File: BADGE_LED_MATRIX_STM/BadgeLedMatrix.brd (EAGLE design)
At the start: 100 x 50 mm, 111 parts, among them CN2 MICRO-USB-5P-340015001, IC1 STM32F0P, IC2 REG1117, Q1 12MHz, Q2 8MHz, U1 USBLC6SOT-23

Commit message: Fix for connection of VCC from shift registers
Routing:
- net BTN3: track 23.1 -> 28.7 mm
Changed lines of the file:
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@@
 <via x="36.83" y="42.545" extent="1-16" drill="0.8" diameter="0.6096"/>
 <wire x1="34.29" y1="16.51" x2="40.005" y2="19.05" width="0.8128" layer="1"/>
-<contactref element="ROWS" pad="16"/>
 <contactref element="ROWS" pad="10"/>
 <wire x1="47.625" y1="15.5" x2="47.625" y2="13.335" width="0.4064" layer="1"/>
-<wire x1="40.005" y1="15.5" x2="40.005" y2="19.05" width="0.4064" layer="1"/>
-<contactref element="COLUMNS" pad="16"/>
 <contactref element="COLUMNS" pad="10"/>
 <wire x1="45.085" y1="42.545" x2="46.99" y2="42.545" width="0.4064" layer="1"/>
@@
 <wire x1="34.29" y1="16.51" x2="34.29" y2="8.89" width="0.8128" layer="1"/>
 <wire x1="32.385" y1="6.985" x2="19.685" y2="6.985" width="0.8128" layer="1"/>
-<wire x1="36.83" y1="42.545" x2="36.83" y2="43.815" width="0.6096" layer="1"/>
-<wire x1="36.83" y1="43.815" x2="38.1" y2="45.085" width="0.6096" layer="1"/>
-<wire x1="38.1" y1="45.085" x2="39.63" y2="45.085" width="0.6096" layer="1"/>
-<wire x1="39.63" y1="45.085" x2="40.005" y2="44.71" width="0.6096" layer="1"/>
+<wire x1="36.83" y1="42.545" x2="36.83" y2="44.03" width="0.6096" layer="1"/>
 <contactref element="PRG" pad="1"/>
 <contactref element="PRG" pad="2"/>
@@
 <wire x1="10.2" y1="22.2" x2="11.595" y2="22.2" width="0.4064" layer="1"/>
 <wire x1="11.595" y1="22.2" x2="16.185" y2="17.61" width="0.4064" layer="1"/>
+<contactref element="COLUMNS" pad="16"/>
+<contactref element="ROWS" pad="16"/>
+<wire x1="36.83" y1="44.03" x2="37.8" y2="45" width="0.6096" layer="1"/>
+<wire x1="37.8" y1="45" x2="39.715" y2="45" width="0.6096" layer="1"/>
+<wire x1="39.715" y1="45" x2="40.005" y2="44.71" width="0.6096" layer="1"/>
+<wire x1="40.005" y1="15.5" x2="40.005" y2="19.05" width="0.6096" layer="1"/>
 </signal>
 <signal name="C0">
@@
 <wire x1="32.385" y1="31.115" x2="31.75" y2="31.75" width="0.3048" layer="1"/>
 <wire x1="31.75" y1="31.75" x2="31.75" y2="41.91" width="0.3048" layer="1"/>
-<wire x1="32.345" y1="14.351" x2="32.345" y2="19.939" width="0" layer="19" extent="1-1"/>
+<wire x1="32.345" y1="19.939" x2="32.345" y2="14.351" width="0.3048" layer="1"/>
 </signal>
 <signal name="BTN4">

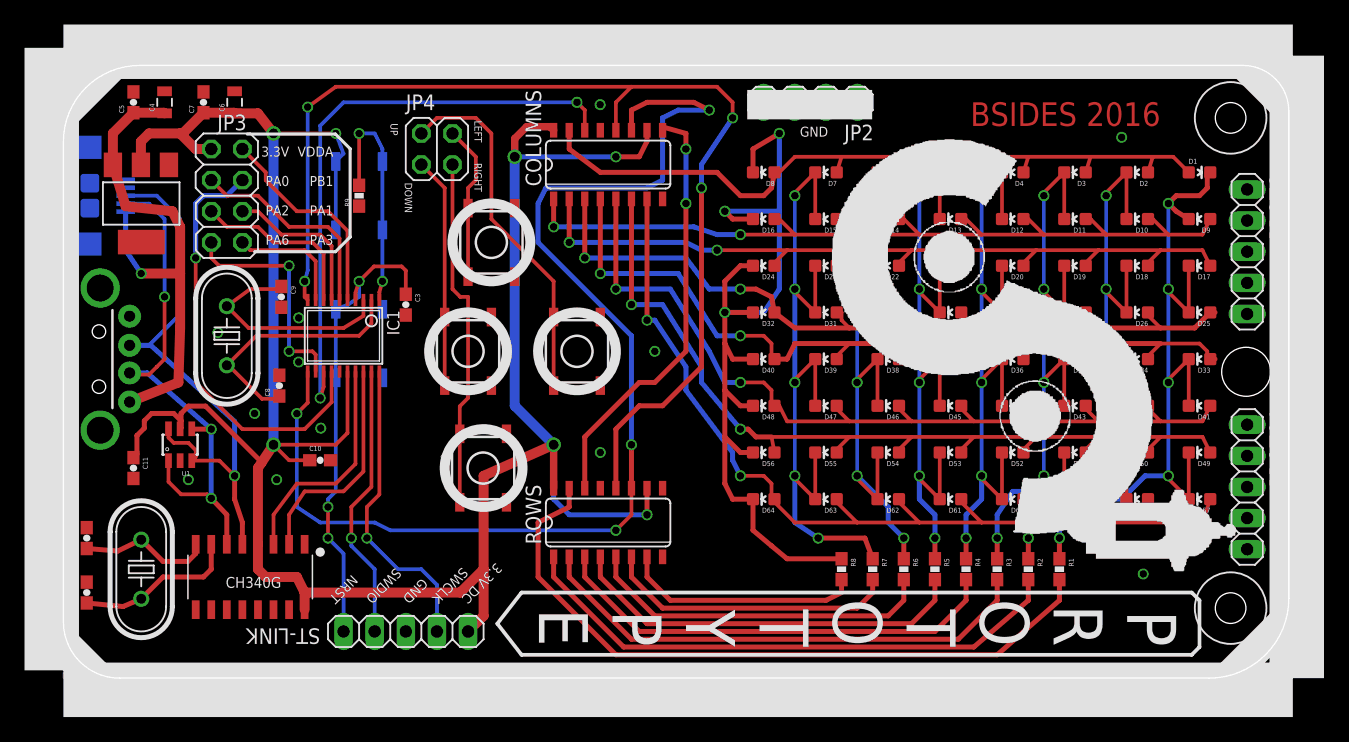
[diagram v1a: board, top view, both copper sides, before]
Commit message: Board diode orientation fix, board corners, allignment of top corner holes
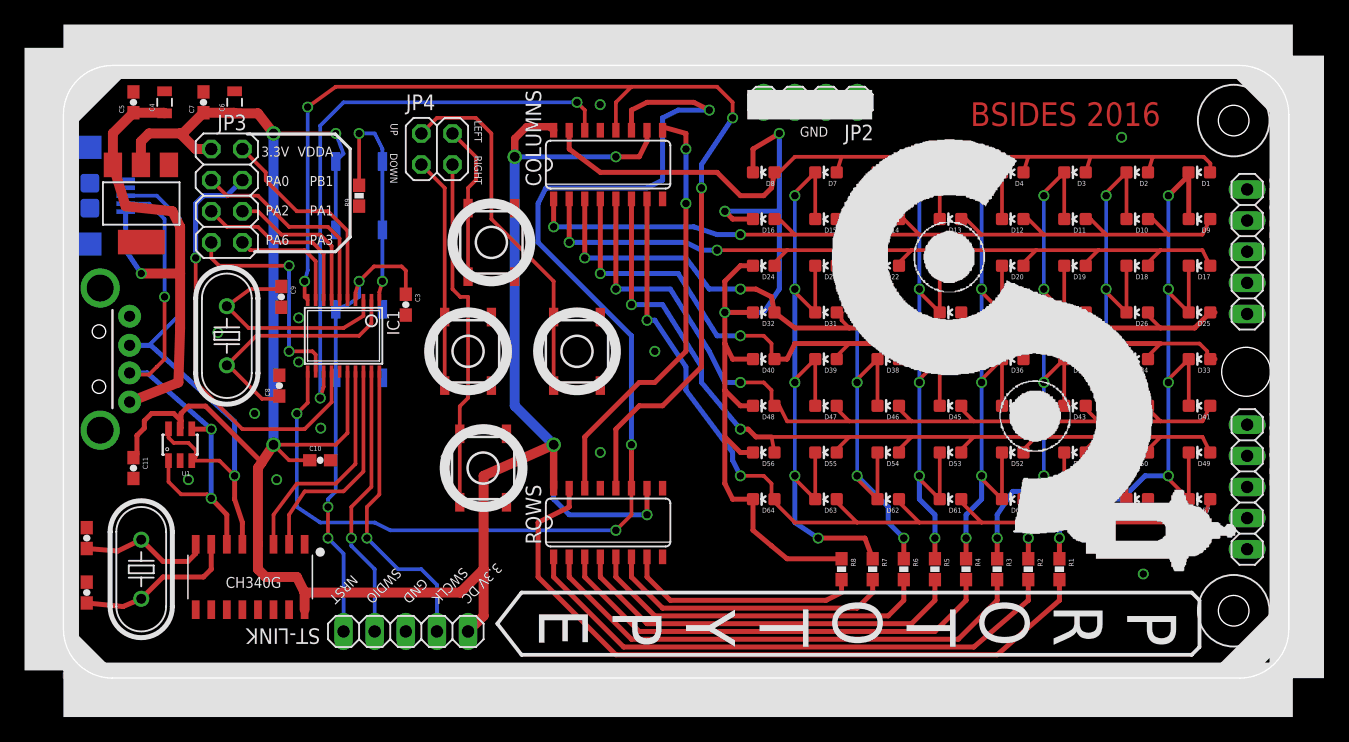
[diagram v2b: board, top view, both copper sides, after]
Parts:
- moved U$5 0.33 mm to (95.5, 45.5)
- moved U$3 0.33 mm to (95.5, 5.50)
- turned D1 to 90 degrees
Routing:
- net C0: track 63.9 -> 66.1 mm
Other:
- outline, holes or cut-outs redrawn
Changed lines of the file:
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@@
 <board>
 <plain>
-<wire x1="4.57905" y1="0" x2="93.494578125" y2="0" width="0" layer="20"/>
-<wire x1="93.494578125" y1="0" x2="100" y2="6.505421875" width="0" layer="20" curve="90"/>
-<wire x1="100" y1="6.505421875" x2="100" y2="46.265809375" width="0" layer="20"/>
-<wire x1="100" y1="46.265809375" x2="96.265809375" y2="50" width="0" layer="20" curve="90"/>
-<wire x1="96.265809375" y1="50" x2="6.2187875" y2="50" width="0" layer="20"/>
-<wire x1="6.2187875" y1="50" x2="0" y2="43.7812125" width="0" layer="20" curve="90"/>
-<wire x1="0" y1="43.7812125" x2="0" y2="4.57905" width="0" layer="20"/>
-<wire x1="0" y1="4.57905" x2="4.57905" y2="0" width="0" layer="20" curve="90"/>
+<wire x1="100" y1="46" x2="96" y2="50" width="0" layer="20" curve="90"/>
+<wire x1="96" y1="50" x2="4" y2="50" width="0" layer="20"/>
+<wire x1="4" y1="50" x2="0" y2="46" width="0" layer="20" curve="90"/>
+<wire x1="0" y1="46" x2="0" y2="4" width="0" layer="20"/>
+<wire x1="0" y1="4" x2="4" y2="0" width="0" layer="20" curve="90"/>
+<wire x1="4" y1="0" x2="96" y2="0" width="0" layer="20"/>
+<wire x1="96" y1="0" x2="100" y2="4" width="0" layer="20" curve="90"/>
+<wire x1="100" y1="4" x2="100" y2="46" width="0" layer="20"/>
 <rectangle x1="0" y1="48.895" x2="100.33" y2="53.34" layer="21"/>
 <rectangle x1="0" y1="-3.175" x2="100.33" y2="1.27" layer="21"/>
@@
 <text x="89.535" y="46.99" size="1.9304" layer="1" font="vector" align="top-right">BSIDES 2016</text>
 <hole x="96.52" y="25" drill="4"/>
-<text x="28.46" y="37.96" size="0.6096" layer="21" rot="SR270" align="top-right">DOWN</text>
+<text x="27.26" y="40.36" size="0.6096" layer="21" rot="SR270" align="top-right">DOWN</text>
 <text x="27.295" y="44.28" size="0.6096" layer="21" rot="SR270" align="top-right">UP</text>
 <text x="34.145" y="43.715" size="0.6096" layer="21" rot="SR270" align="top-right">LEFT</text>
-<text x="34.145" y="39.69" size="0.6096" layer="21" rot="SR270" align="top-right">RIGHT</text>
+<text x="34.145" y="40.29" size="0.6096" layer="21" rot="SR270" align="top-right">RIGHT</text>
 <text x="22.2" y="6" size="0.8128" layer="21" rot="SR225" align="top-right">NRST</text>
 <text x="25.2" y="6" size="0.8128" layer="21" rot="SR225" align="top-right">SWDIO</text>
@@
 </autorouter>
 <elements>
-<element name="D1" library="SparkFun-LED" package="LED-0603" value="" x="92.71" y="41.275" rot="R270"/>
+<element name="D1" library="SparkFun-LED" package="LED-0603" value="" x="92.69" y="41.275" rot="R90"/>
 <element name="D2" library="SparkFun-LED" package="LED-0603" value="" x="87.63" y="41.275" rot="R90"/>
 <element name="D3" library="SparkFun-LED" package="LED-0603" value="" x="82.55" y="41.275" rot="R90"/>
@@
 <element name="C10" library="SparkFun-Capacitors" package="0603-CAP" value="100nF" x="20.955" y="17.78"/>
 <element name="C11" library="SparkFun-Capacitors" package="0603-CAP" value="4.7uF" x="5.715" y="17.145" rot="R270"/>
-<element name="U$5" library="special" package="DRIL-2,5" value="" x="95.25" y="45.72"/>
-<element name="U$3" library="special" package="DRIL-2,5" value="" x="95.25" y="5.715"/>
+<element name="U$5" library="special" package="DRIL-2,5" value="" x="95.5" y="45.5"/>
+<element name="U$3" library="special" package="DRIL-2,5" value="" x="95.5" y="5.5"/>
 <element name="U$4" library="logo" package="RADIOACTIVE" value="" x="33.655" y="14.605" rot="MR90"/>
 <element name="JP4" library="pinhead" package="2X02" value="" x="30.48" y="43.18"/>
@@
 <wire x1="78.74" y1="42.545" x2="83.82" y2="42.545" width="0.3048" layer="1"/>
 <wire x1="83.82" y1="42.545" x2="88.9" y2="42.545" width="0.3048" layer="1"/>
-<wire x1="88.9" y1="42.545" x2="90.563" y2="42.545" width="0.3048" layer="1"/>
-<wire x1="90.563" y1="42.545" x2="91.833" y2="41.275" width="0.3048" layer="1"/>
 <wire x1="83.427" y1="41.275" x2="83.82" y2="42.545" width="0.3048" layer="1"/>
 <wire x1="63.107" y1="41.275" x2="63.5" y2="42.545" width="0.3048" layer="1"/>
@@
 <contactref element="COLUMNS" pad="15"/>
 <wire x1="41.275" y1="43.18" x2="41.275" y2="44.71" width="0.4064" layer="1"/>
+<wire x1="88.9" y1="42.545" x2="93.055" y2="42.545" width="0.3048" layer="1"/>
+<wire x1="93.055" y1="42.545" x2="93.6" y2="42" width="0.3048" layer="1"/>
+<wire x1="93.6" y1="42" x2="93.6" y2="41.308" width="0.3048" layer="1"/>
+<wire x1="93.6" y1="41.308" x2="93.567" y2="41.275" width="0.3048" layer="1"/>
 </signal>
 <signal name="R0">
@@
 <wire x1="90.17" y1="16.51" x2="90.17" y2="24.13" width="0.3048" layer="16"/>
 <via x="90.17" y="24.13" extent="1-16" drill="0.6096"/>
-<wire x1="90.17" y1="31.75" x2="90.17" y2="38.735" width="0.3048" layer="16"/>
-<via x="90.17" y="38.735" extent="1-16" drill="0.6096"/>
+<wire x1="90.17" y1="31.75" x2="90.17" y2="39.37" width="0.3048" layer="16"/>
+<via x="90.17" y="39.37" extent="1-16" drill="0.6096"/>
 <contactref element="R1" pad="1"/>
 <wire x1="81.28" y1="9.74" x2="81.28" y2="11.43" width="0.4064" layer="1"/>
@@
 <via x="90.17" y="31.75" extent="1-16" drill="0.6096"/>
 <wire x1="90.17" y1="31.75" x2="90.17" y2="24.13" width="0.3048" layer="16"/>
-<wire x1="91.833" y1="37.465" x2="90.805" y2="38.1" width="0.4064" layer="1"/>
-<wire x1="90.805" y1="38.1" x2="90.17" y2="38.735" width="0.4064" layer="1"/>
-<wire x1="93.587" y1="41.275" x2="93.345" y2="41.275" width="0.4064" layer="1"/>
-<wire x1="93.345" y1="41.275" x2="93.345" y2="40.005" width="0.4064" layer="1"/>
-<wire x1="93.345" y1="40.005" x2="92.71" y2="39.37" width="0.4064" layer="1"/>
-<wire x1="92.71" y1="39.37" x2="90.805" y2="39.37" width="0.4064" layer="1"/>
-<wire x1="90.805" y1="39.37" x2="90.17" y2="38.735" width="0.4064" layer="1"/>
 <wire x1="90.17" y1="16.51" x2="90.17" y2="16.268" width="0.3048" layer="1"/>
 <wire x1="90.17" y1="16.268" x2="91.833" y2="14.605" width="0.3048" layer="1"/>
@@
 <wire x1="90.17" y1="24.13" x2="90.17" y2="24.372" width="0.3048" layer="1"/>
 <wire x1="90.17" y1="24.372" x2="91.833" y2="26.035" width="0.3048" layer="1"/>
+<wire x1="91.813" y1="41.275" x2="91.813" y2="41.013" width="0.4064" layer="1"/>
+<wire x1="91.813" y1="41.013" x2="90.17" y2="39.37" width="0.4064" layer="1"/>
+<wire x1="91.833" y1="37.465" x2="91.833" y2="41.255" width="0.4064" layer="1"/>
+<wire x1="91.833" y1="41.255" x2="91.813" y2="41.275" width="0.4064" layer="1"/>
 </signal>
 <signal name="R1IN">

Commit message: Fixing board white border, top and bottom
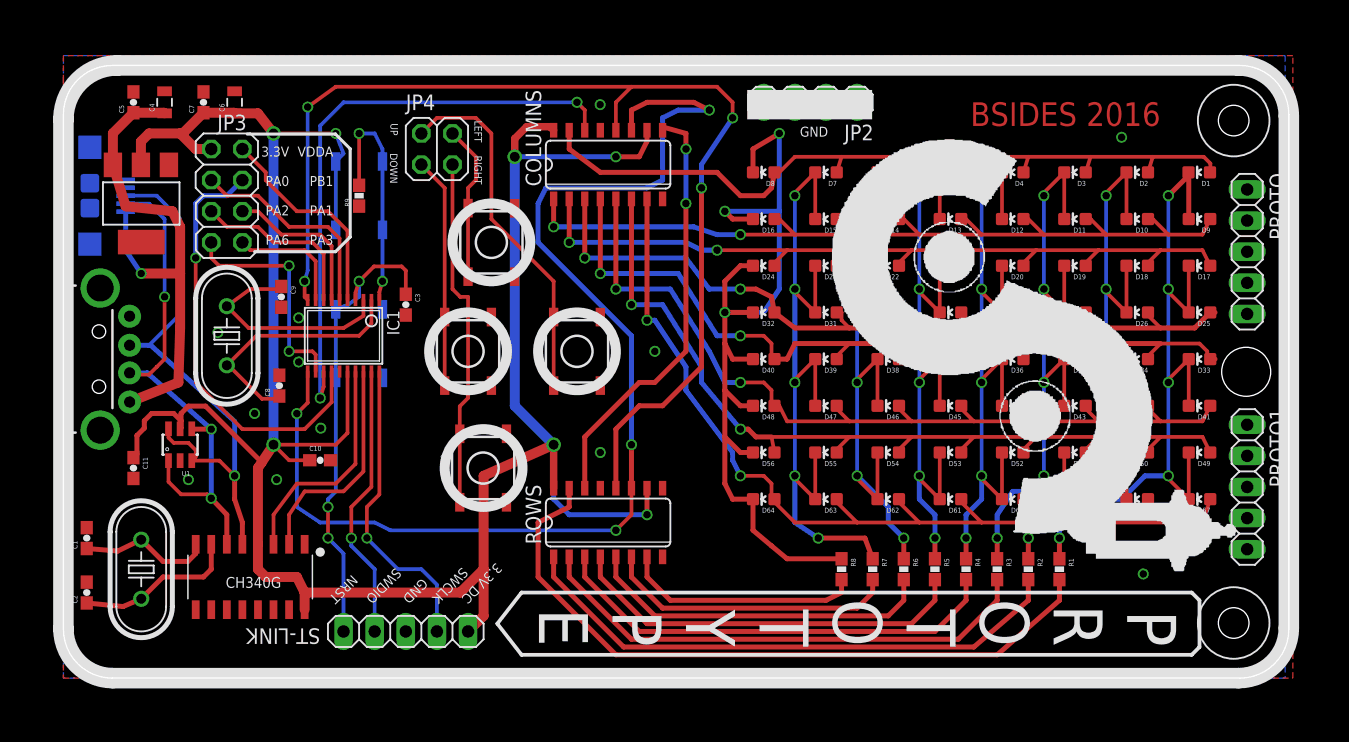
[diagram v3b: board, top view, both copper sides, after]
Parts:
- moved U$3 1.00 mm to (95.5, 4.50)
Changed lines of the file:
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@@
 <wire x1="96" y1="0" x2="100" y2="4" width="0" layer="20" curve="90"/>
 <wire x1="100" y1="4" x2="100" y2="46" width="0" layer="20"/>
-<rectangle x1="0" y1="48.895" x2="100.33" y2="53.34" layer="21"/>
-<rectangle x1="0" y1="-3.175" x2="100.33" y2="1.27" layer="21"/>
-<rectangle x1="98.425" y1="0" x2="102.87" y2="50.8" layer="21"/>
-<rectangle x1="-3.175" y1="0.635" x2="1.27" y2="51.435" layer="21"/>
-<rectangle x1="-0.991021875" y1="47.21450625" x2="5.993978125" y2="49.75450625" layer="21" rot="R45"/>
-<rectangle x1="93.623978125" y1="0.85950625" x2="100.608978125" y2="3.39950625" layer="21" rot="R45"/>
-<rectangle x1="94.70799375" y1="46.951478125" x2="101.69299375" y2="49.491478125" layer="21" rot="R135"/>
-<rectangle x1="-1.81200625" y1="-0.038521875" x2="5.17299375" y2="2.501478125" layer="21" rot="R135"/>
 <circle x="33.02" y="26.67" radius="3.175" width="0.8128" layer="21"/>
 <circle x="34.925" y="35.56" radius="3.175" width="0.8128" layer="21"/>
@@
 <rectangle x1="55.8" y1="45.6" x2="66" y2="48" layer="21"/>
 <text x="62.4" y="45" size="0.8128" layer="21" align="top-right">GND</text>
+<wire x1="100" y1="45.876896875" x2="100" y2="4.10365625" width="1.6764" layer="21"/>
+<wire x1="100" y1="4.10365625" x2="95.89634375" y2="0" width="1.6764" layer="21" curve="-90"/>
+<wire x1="95.89634375" y1="0" x2="4.024921875" y2="0" width="1.6764" layer="21"/>
+<wire x1="4.024921875" y1="0" x2="0" y2="4.024921875" width="1.6764" layer="21" curve="-90"/>
+<wire x1="0" y1="4.024921875" x2="0" y2="45.613659375" width="1.6764" layer="21"/>
+<wire x1="0" y1="45.613659375" x2="4.386340625" y2="50" width="1.6764" layer="21" curve="-90"/>
+<wire x1="4.386340625" y1="50" x2="95.876896875" y2="50" width="1.6764" layer="21"/>
+<wire x1="95.876896875" y1="50" x2="100" y2="45.876896875" width="1.6764" layer="21" curve="-90"/>
+<wire x1="100" y1="45.876896875" x2="100" y2="4.10365625" width="1.6764" layer="22"/>
+<wire x1="100" y1="4.10365625" x2="95.89634375" y2="0" width="1.6764" layer="22" curve="-90"/>
+<wire x1="95.89634375" y1="0" x2="4.024921875" y2="0" width="1.6764" layer="22"/>
+<wire x1="4.024921875" y1="0" x2="0" y2="4.024921875" width="1.6764" layer="22" curve="-90"/>
+<wire x1="0" y1="4.024921875" x2="0" y2="45.613659375" width="1.6764" layer="22"/>
+<wire x1="0" y1="45.613659375" x2="4.386340625" y2="50" width="1.6764" layer="22" curve="-90"/>
+<wire x1="4.386340625" y1="50" x2="95.876896875" y2="50" width="1.6764" layer="22"/>
+<wire x1="95.876896875" y1="50" x2="100" y2="45.876896875" width="1.6764" layer="22" curve="-90"/>
 </plain>
 <attributes>
@@
 <element name="C11" library="SparkFun-Capacitors" package="0603-CAP" value="4.7uF" x="5.715" y="17.145" rot="R270"/>
 <element name="U$5" library="special" package="DRIL-2,5" value="" x="95.5" y="45.5"/>
-<element name="U$3" library="special" package="DRIL-2,5" value="" x="95.5" y="5.5"/>
+<element name="U$3" library="special" package="DRIL-2,5" value="" x="95.5" y="4.5"/>
 <element name="U$4" library="logo" package="RADIOACTIVE" value="" x="33.655" y="14.605" rot="MR90"/>
 <element name="JP4" library="pinhead" package="2X02" value="" x="30.48" y="43.18"/>

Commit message: Added EPROM and wired up buttons
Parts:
- removed JP3: (no value), pinhead:2X04
- removed JP4: (no value), pinhead:2X02
- added U$6: AT93C66A, digital-ic:SOP-8
- moved R9 0.50 mm to (24.1, 39.9)
- renumbered BTN1 to UP, BTN2 to LEFT, BTN3 to RIGHT, BTN4 to DOWN
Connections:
- removed net BTN1: JP4.2, UP.1, UP.2
- removed net BTN2: JP4.4, LEFT.1, LEFT.2
- removed net BTN3: JP4.3, RIGHT.1, RIGHT.2
- removed net BTN4: DOWN.1, DOWN.2, JP4.1
- net CLK_MCU: now also U$6.PIN2
- net GND: now also U$6.PIN5
- net PA0: now also UP.1, UP.2; no longer JP3.3
- net PA1: now also LEFT.1, LEFT.2; no longer JP3.6
- net PA2: now also RIGHT.1, RIGHT.2; no longer JP3.5
- net PA3: now also U$6.PIN1; no longer JP3.8
- net PA6: now also U$6.PIN4; no longer JP3.7
- net PB1: now also DOWN.1, DOWN.2; no longer JP3.4
- net SER_DATA: now also U$6.PIN3
- net VCC: now also U$6.PIN6, U$6.PIN8; no longer JP3.1
- net VDDA: no longer JP3.2
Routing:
- net BTN1: track 29.4 -> 0.00 mm
- net BTN3: track 28.7 -> 0.00 mm
- net CLK_MCU: track 97.1 -> 117.5 mm, vias 4 -> 5
- net PA2: track 14.4 -> 33.9 mm, vias 0 -> 2
- net BTN4: track 18.8 -> 0.00 mm
- net PB1: track 35.3 -> 17.5 mm, vias 1 -> 0
- net VDDA: track 17.4 -> 0.00 mm
- net SER_DATA: track 48.7 -> 63.7 mm, vias 2 -> 3
- net PA3: track 9.78 -> 23.7 mm
- net BTN2: track 12.7 -> 0.00 mm
- net PA0: track 17.5 -> 27.2 mm
- net PA6: track 18.5 -> 26.8 mm
- net PA1: track 12.9 -> 20.6 mm
- net N$4: track 19.3 -> 15.7 mm
- net VCC: track 200.8 -> 204.1 mm
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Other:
- board text added: "BSIDES"
- board text added: "Puerto Rico"
- board text added: "Security"
- board text added: "VCC"
- board text removed: "3.3V"
- board text removed: "3.3V DC"
- board text removed: "DOWN"
- board text removed: "LEFT"
- board text removed: "PA0"
- board text removed: "PA1"
- board text removed: "PA2"
- board text removed: "PA3"
- board text removed: "PA6"
- board text removed: "PB1"
- board text removed: "RIGHT"
- board text removed: "UP"
- board text removed: "VDDA"
